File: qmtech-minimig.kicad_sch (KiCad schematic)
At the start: 0 parts

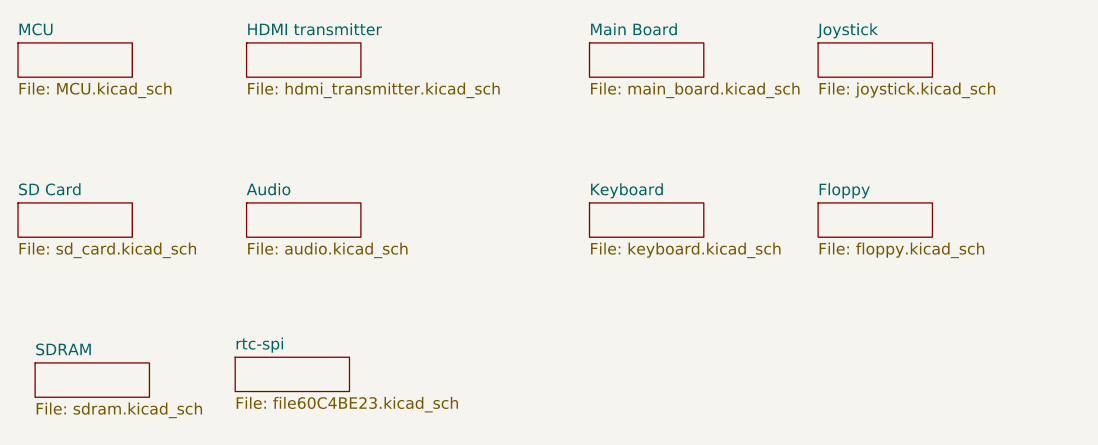
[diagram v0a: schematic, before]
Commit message: Prod version of OpenAARS 5.0 design.
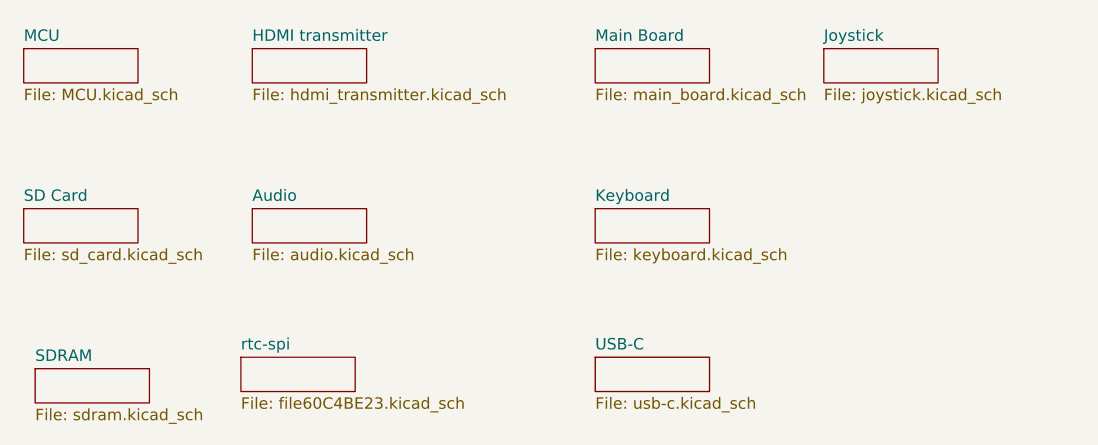
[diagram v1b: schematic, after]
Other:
- removed sheet Floppy
- added sheet USB-C (usb-c.kicad_sch)
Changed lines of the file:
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@@
     (company "deFEEST")
   )
-  (sheet (at 46.355 38.735) (size 12.7 3.81) (fields_autoplaced)
+  (sheet (at 46.99 39.37) (size 12.7 3.81) (fields_autoplaced)
     (stroke (width 0) (type solid))
     (fill (color 0 0 0 0.0000))
-    (property "Sheetname" "MCU" (at 46.355 38.0234 0)
+    (property "Sheetname" "MCU" (at 46.99 38.6584 0)
       (effects (font (size 1.27 1.27)) (justify left bottom))
     )
-    (property "Sheetfile" "MCU.kicad_sch" (at 46.355 43.1296 0)
+    (property "Sheetfile" "MCU.kicad_sch" (at 46.99 43.7646 0)
       (effects (font (size 1.27 1.27)) (justify left top))
     )
     (instances
       (project "qmtech-minimig"
-        (path "/c3d5daf8-d359-42b2-a7c2-0d080ba7e212" (page "7"))
+        (path "/c3d5daf8-d359-42b2-a7c2-0d080ba7e212" (page "13"))
       )
     )
   )
-  (sheet (at 71.755 38.735) (size 12.7 3.81) (fields_autoplaced)
+  (sheet (at 72.39 39.37) (size 12.7 3.81) (fields_autoplaced)
     (stroke (width 0) (type solid))
     (fill (color 0 0 0 0.0000))
-    (property "Sheetname" "HDMI transmitter" (at 71.755 38.0234 0)
+    (property "Sheetname" "HDMI transmitter" (at 72.39 38.6584 0)
       (effects (font (size 1.27 1.27)) (justify left bottom))
     )
-    (property "Sheetfile" "hdmi_transmitter.kicad_sch" (at 71.755 43.1296 0)
+    (property "Sheetfile" "hdmi_transmitter.kicad_sch" (at 72.39 43.7646 0)
       (effects (font (size 1.27 1.27)) (justify left top))
     )
@@
     )
   )
-  (sheet (at 109.855 38.735) (size 12.7 3.81) (fields_autoplaced)
+  (sheet (at 110.49 39.37) (size 12.7 3.81) (fields_autoplaced)
     (stroke (width 0) (type solid))
     (fill (color 0 0 0 0.0000))
-    (property "Sheetname" "Main Board" (at 109.855 38.0234 0)
+    (property "Sheetname" "Main Board" (at 110.49 38.6584 0)
       (effects (font (size 1.27 1.27)) (justify left bottom))
     )
-    (property "Sheetfile" "main_board.kicad_sch" (at 109.855 43.1296 0)
+    (property "Sheetfile" "main_board.kicad_sch" (at 110.49 43.7646 0)
       (effects (font (size 1.27 1.27)) (justify left top))
     )
@@
     )
   )
-  (sheet (at 135.255 38.735) (size 12.7 3.81) (fields_autoplaced)
+  (sheet (at 135.89 39.37) (size 12.7 3.81) (fields_autoplaced)
     (stroke (width 0) (type solid))
     (fill (color 0 0 0 0.0000))
-    (property "Sheetname" "Joystick" (at 135.255 38.0234 0)
+    (property "Sheetname" "Joystick" (at 135.89 38.6584 0)
       (effects (font (size 1.27 1.27)) (justify left bottom))
     )
-    (property "Sheetfile" "joystick.kicad_sch" (at 135.255 43.1296 0)
+    (property "Sheetfile" "joystick.kicad_sch" (at 135.89 43.7646 0)
       (effects (font (size 1.27 1.27)) (justify left top))
     )
@@
     )
   )
-  (sheet (at 46.355 56.515) (size 12.7 3.81) (fields_autoplaced)
+  (sheet (at 46.99 57.15) (size 12.7 3.81) (fields_autoplaced)
     (stroke (width 0) (type solid))
     (fill (color 0 0 0 0.0000))
-    (property "Sheetname" "SD Card" (at 46.355 55.8034 0)
+    (property "Sheetname" "SD Card" (at 46.99 56.4384 0)
       (effects (font (size 1.27 1.27)) (justify left bottom))
     )
-    (property "Sheetfile" "sd_card.kicad_sch" (at 46.355 60.9096 0)
+    (property "Sheetfile" "sd_card.kicad_sch" (at 46.99 61.5446 0)
       (effects (font (size 1.27 1.27)) (justify left top))
     )
@@
     )
   )
-  (sheet (at 71.755 56.515) (size 12.7 3.81) (fields_autoplaced)
+  (sheet (at 72.39 57.15) (size 12.7 3.81) (fields_autoplaced)
     (stroke (width 0) (type solid))
     (fill (color 0 0 0 0.0000))
-    (property "Sheetname" "Audio" (at 71.755 55.8034 0)
+    (property "Sheetname" "Audio" (at 72.39 56.4384 0)
       (effects (font (size 1.27 1.27)) (justify left bottom))
     )
-    (property "Sheetfile" "audio.kicad_sch" (at 71.755 60.9096 0)
+    (property "Sheetfile" "audio.kicad_sch" (at 72.39 61.5446 0)
       (effects (font (size 1.27 1.27)) (justify left top))
     )
@@
     )
   )
-  (sheet (at 109.855 56.515) (size 12.7 3.81) (fields_autoplaced)
+  (sheet (at 110.49 57.15) (size 12.7 3.81) (fields_autoplaced)
     (stroke (width 0) (type solid))
     (fill (color 0 0 0 0.0000))
-    (property "Sheetname" "Keyboard" (at 109.855 55.8034 0)
+    (property "Sheetname" "Keyboard" (at 110.49 56.4384 0)
       (effects (font (size 1.27 1.27)) (justify left bottom))
     )
-    (property "Sheetfile" "keyboard.kicad_sch" (at 109.855 60.9096 0)
+    (property "Sheetfile" "keyboard.kicad_sch" (at 110.49 61.5446 0)
       (effects (font (size 1.27 1.27)) (justify left top))
     )
@@
     )
   )
-  (sheet (at 135.255 56.515) (size 12.7 3.81) (fields_autoplaced)
+  (sheet (at 48.26 74.93) (size 12.7 3.81) (fields_autoplaced)
     (stroke (width 0) (type solid))
     (fill (color 0 0 0 0.0000))
-    (property "Sheetname" "Floppy" (at 135.255 55.8034 0)
+    (property "Sheetname" "SDRAM" (at 48.26 74.2184 0)
       (effects (font (size 1.27 1.27)) (justify left bottom))
     )
-    (property "Sheetfile" "floppy.kicad_sch" (at 135.255 60.9096 0)
-      (effects (font (size 1.27 1.27)) (justify left top))
-    )
-    (instances
-      (project "qmtech-minimig"
-        (path "/c3d5daf8-d359-42b2-a7c2-0d080ba7e212" (page "3"))
-      )
-    )
-  )
-  (sheet (at 48.26 74.295) (size 12.7 3.81) (fields_autoplaced)
-    (stroke (width 0) (type solid))
-    (fill (color 0 0 0 0.0000))
-    (property "Sheetname" "SDRAM" (at 48.26 73.5834 0)
-      (effects (font (size 1.27 1.27)) (justify left bottom))
-    )
-    (property "Sheetfile" "sdram.kicad_sch" (at 48.26 78.6896 0)
+    (property "Sheetfile" "sdram.kicad_sch" (at 48.26 79.3246 0)
       (effects (font (size 1.27 1.27)) (justify left top))
     )
@@
     )
   )
-  (sheet (at 70.485 73.66) (size 12.7 3.81) (fields_autoplaced)
+  (sheet (at 71.12 73.66) (size 12.7 3.81) (fields_autoplaced)
     (stroke (width 0) (type solid))
     (fill (color 0 0 0 0.0000))
-    (property "Sheetname" "rtc-spi" (at 70.485 72.9484 0)
+    (property "Sheetname" "rtc-spi" (at 71.12 72.9484 0)
       (effects (font (size 1.27 1.27)) (justify left bottom))
     )
-    (property "Sheetfile" "file60C4BE23.kicad_sch" (at 70.485 78.0546 0)
+    (property "Sheetfile" "file60C4BE23.kicad_sch" (at 71.12 78.0546 0)
       (effects (font (size 1.27 1.27)) (justify left top))
     )
@@
       )
     )
+  )
+  (sheet (at 110.49 73.66) (size 12.7 3.81) (fields_autoplaced)
+    (stroke (width 0.1524) (type solid))
+    (fill (color 0 0 0 0.0000))
+    (property "Sheetname" "USB-C" (at 110.49 72.9484 0)
+      (effects (font (size 1.27 1.27)) (justify left bottom))
+    )
+    (property "Sheetfile" "usb-c.kicad_sch" (at 110.49 78.0546 0)
+      (effects (font (size 1.27 1.27)) (justify left top))
+    )
+    (instances
+      (project "qmtech-minimig"
+        (path "/c3d5daf8-d359-42b2-a7c2-0d080ba7e212" (page "12"))
+      )
+    )
